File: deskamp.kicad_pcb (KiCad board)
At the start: 2 copper layers, 28 parts, among them J1 Input 01, J2 Input 02, J3 Preamp Out, J4 Selector Switch, J5 LFE, J6 Mute, J7 Sleep, J8 Motor, J9 Power, K1 Mute, K2 Sleep, K3 TQ2-12V, K4 TQ2-12V, Q1 PN2222A, Q2 PN2222A, Q3 PN2222A, Q4 PN2222A, U1 esp32-wemos-d1-mini, U2 L9110, U3 TSR_1-2433

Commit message: Stuck until modelling Alps pot
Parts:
- K1: value Mute -> TQ2-12V; footprint Relay_THT:Relay_SPDT_Panasonic_JW1_FormC -> tq2:RELAY_TQ2_PAN
- K2: value Sleep -> TQ2-12V; footprint Relay_THT:Relay_SPDT_Panasonic_JW1_FormC -> tq2:RELAY_TQ2_PAN
- moved U1 151.5 mm to (188.9, 89.1)
- moved D4 149.7 mm to (189.9, 27.0)
- moved D3 135.3 mm to (175.4, 27.0)
- moved D2 121.1 mm to (160.9, 27.0)
- moved D1 106.9 mm to (146.2, 27.0)
- moved Q4 97.4 mm to (194.2, 51.3)
- moved K4 86.1 mm to (191.4, 33.4)
- moved K3 84.0 mm to (176.8, 33.4)
- moved Q3 81.6 mm to (179.5, 52.5)
- moved U2 79.6 mm to (145.0, 111.5)
- moved K2 76.7 mm to (162.2, 33.5)
- moved U3 74.2 mm to (155.6, 85.8)
- moved R3 69.5 mm to (135.2, 88.0)
- moved Q2 67.7 mm to (165.0, 52.0)
- moved R4 66.6 mm to (133.2, 94.0)
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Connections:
- K1 pad 1: (no net) -> +12V
- K1 pad 2: (no net) -> unconnected-(K1-Pad2)
- K1 pad 4: (no net) -> Net-(J6-Pin_1)
- K1 pad 6: (no net) -> unconnected-(K1-Pad6)
- K1 pad 8: (no net) -> unconnected-(K1-Pad8)
- K2 pad 1: (no net) -> +12V
- K2 pad 2: (no net) -> Net-(J7-Pin_1)
- K2 pad 4: (no net) -> unconnected-(K2-Pad4)
- K2 pad 6: (no net) -> unconnected-(K2-Pad6)
- K2 pad 8: (no net) -> unconnected-(K2-Pad8)
- U1 pad 25: Net-(Q3-B) -> Net-(Q4-B)
- U1 pad 27: Net-(Q4-B) -> Net-(Q3-B)

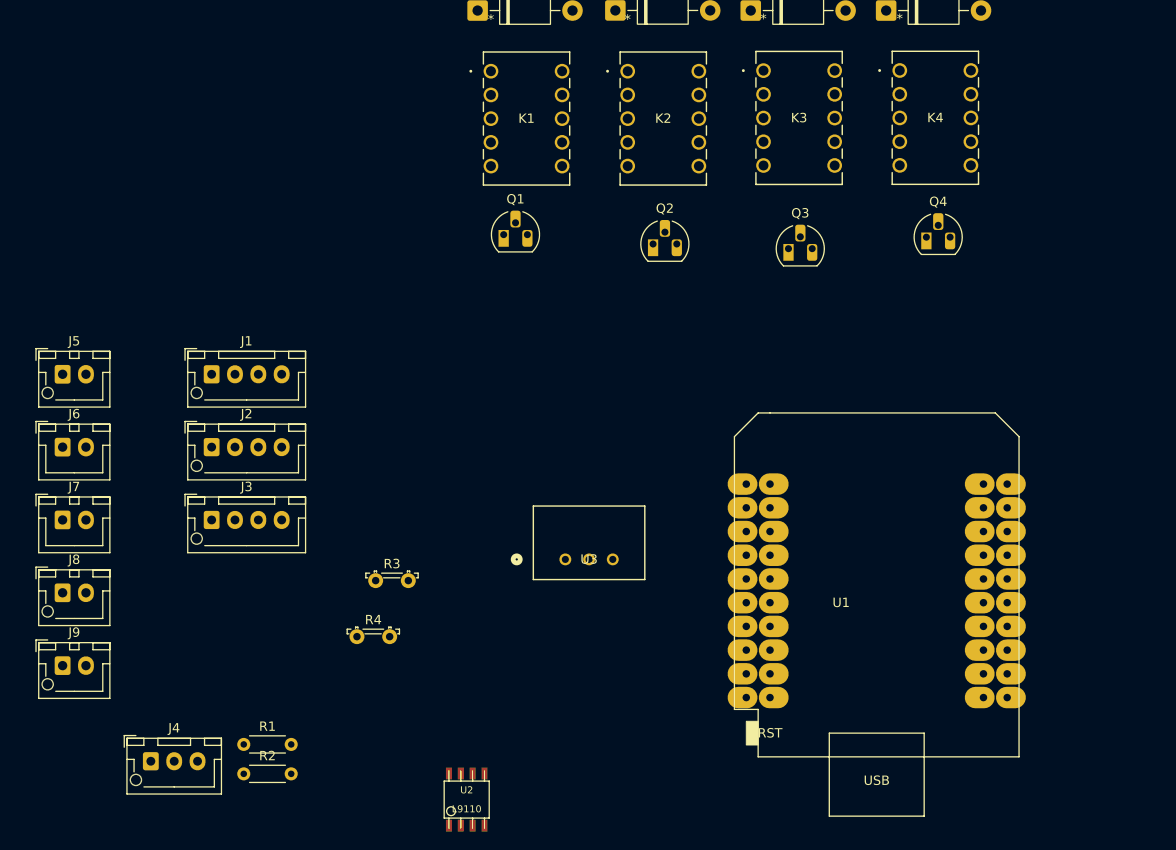
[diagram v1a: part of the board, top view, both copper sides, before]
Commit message: Use Alps RK27 as temp
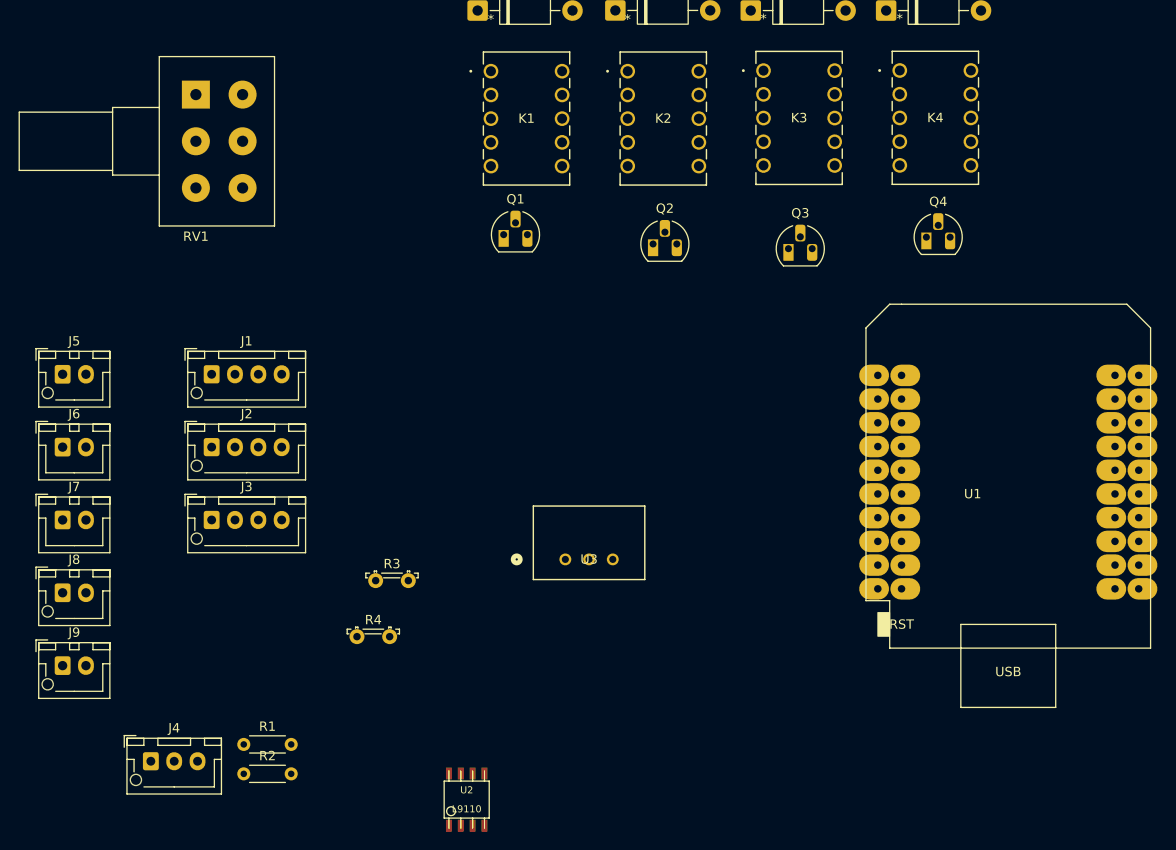
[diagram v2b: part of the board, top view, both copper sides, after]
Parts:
- added RV1: ALPS RK27, Potentiometer_THT:Potentiometer_Alps_RK163_Dual_Horizontal, F.Cu at (116.0, 36.0)
- moved U1 18.3 mm to (203.0, 77.5)

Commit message: Update deskamp.kicad_pcb
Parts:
- moved U2 79.2 mm to (98.6, 47.3)
- moved R2 75.7 mm to (97.5, 36.9)
- moved J4 75.7 mm to (87.5, 35.5)
- moved R1 75.7 mm to (97.5, 33.7)
- moved J9 53.5 mm to (155.0, 92.5)
- moved J8 44.5 mm to (88.2, 47.0)
- moved RV1 41.0 mm to (75.0, 36.2)
- moved J5 23.5 mm to (124.5, 71.8)
- moved J1 21.3 mm to (138.8, 63.0)
- moved J2 21.3 mm to (138.8, 70.8)
- moved J3 19.9 mm to (124.4, 62.9)
- moved U1 9.36 mm to (194.5, 73.5), turned to -90 degrees
- moved Q3 1.50 mm to (179.5, 51.0)
- moved Q2 1.00 mm to (165.0, 51.0)
- moved Q4 0.27 mm to (194.2, 51.0)

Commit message: More arranging
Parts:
- moved R3 59.9 mm to (75.8, 95.0), turned to 180 degrees
- moved R4 57.8 mm to (75.8, 100.0), turned to 180 degrees
- moved J3 54.0 mm to (72.5, 77.5)
- moved J5 54.0 mm to (72.6, 86.4)
- moved J1 16.5 mm to (124.2, 70.8)

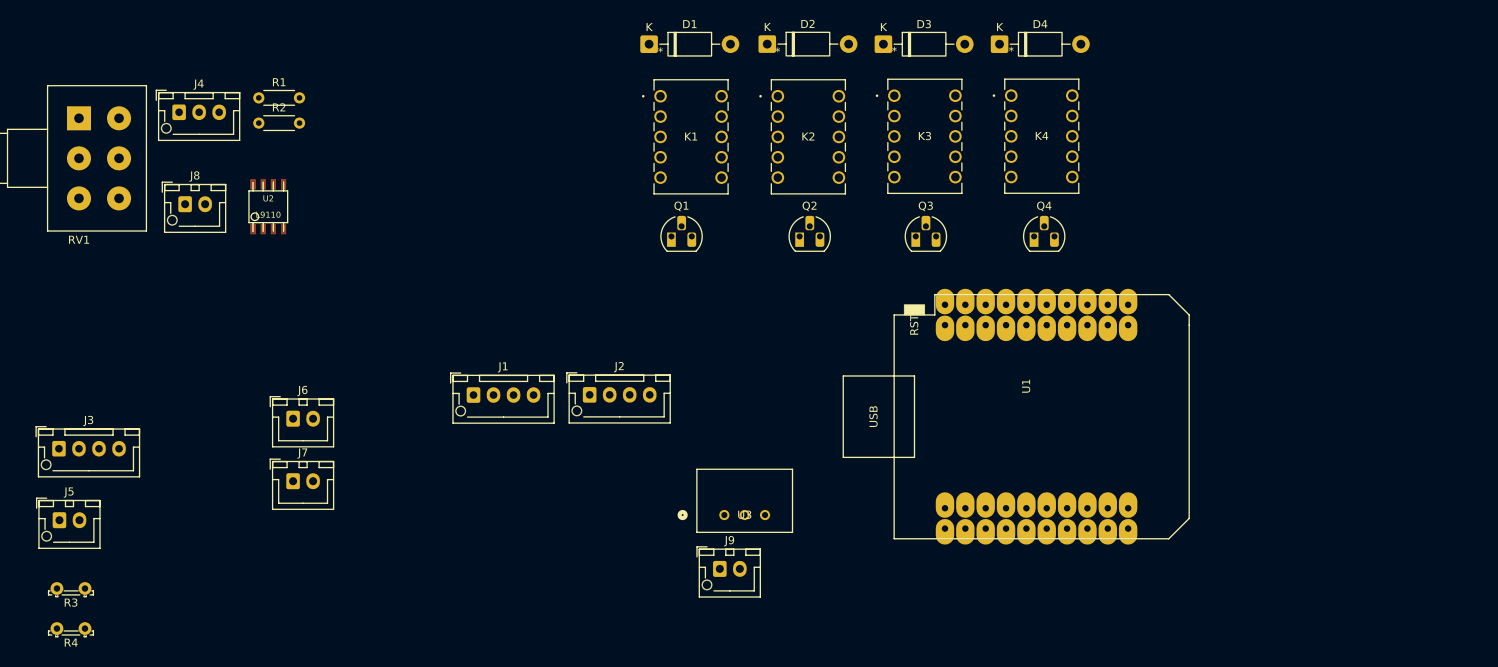
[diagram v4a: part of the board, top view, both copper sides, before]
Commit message: Add base resistors
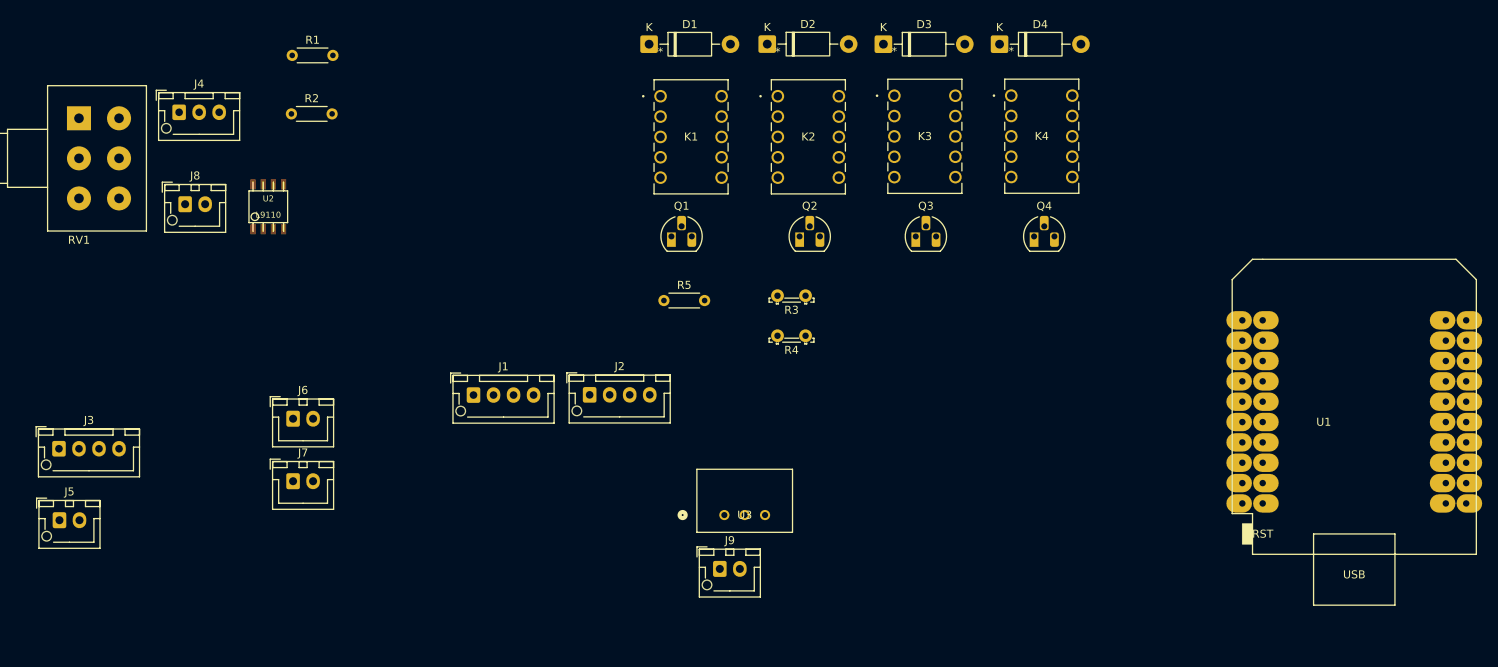
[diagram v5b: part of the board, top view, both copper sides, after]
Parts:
- added R5: 1K, Resistor_THT:R_Axial_DIN0204_L3.6mm_D1.6mm_P5.08mm_Horizontal, F.Cu at (148.0, 59.0)
- moved R3 97.1 mm to (165.7, 58.4)
- moved R4 97.1 mm to (165.7, 63.4)
- moved U1 39.7 mm to (234.2, 72.9), turned to 0 degrees
- moved R1 6.74 mm to (101.6, 28.4)
- moved R2 4.23 mm to (101.5, 35.7)
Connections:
- U1 pad 25: Net-(Q4-B) -> Net-(U1-IO_22/D1/SCL)
- U1 pad 27: Net-(Q3-B) -> Net-(U1-IO_21/D2/SDA)
- U1 pad 29: Net-(Q2-B) -> Net-(U1-IO_17/D3)
- U1 pad 31: Net-(Q1-B) -> Net-(U1-IO_16/D4)

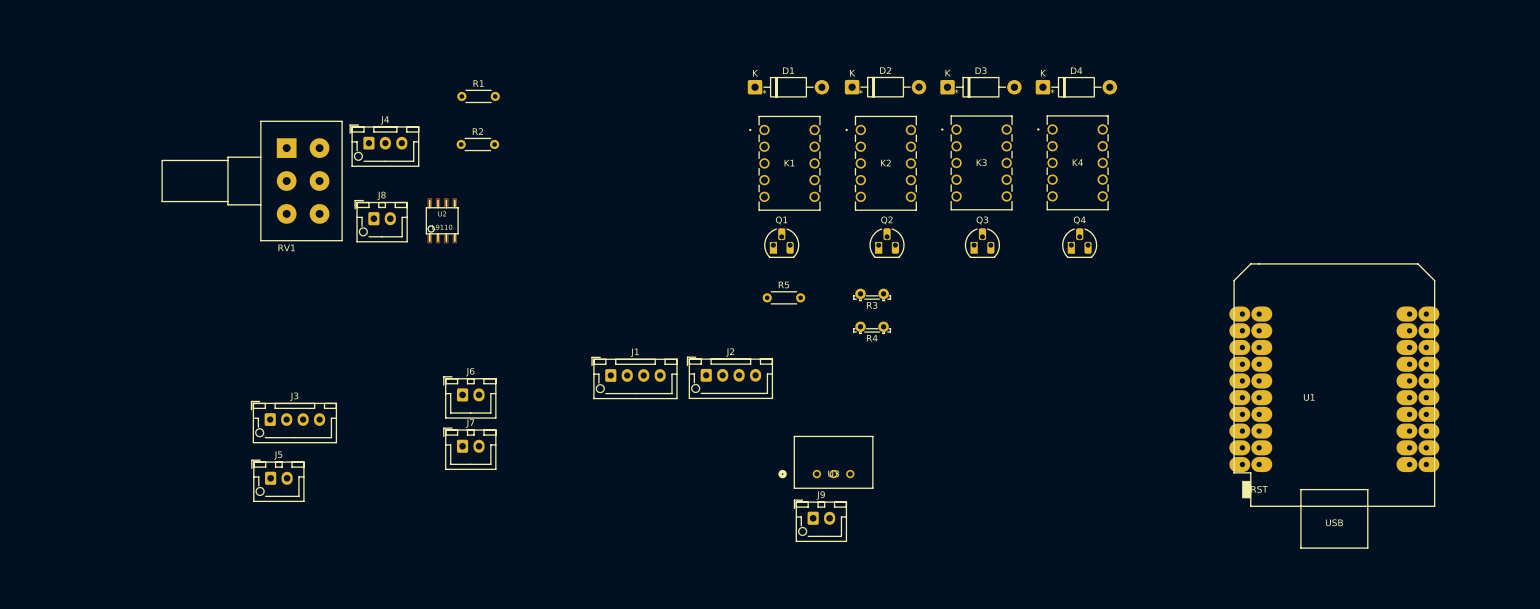
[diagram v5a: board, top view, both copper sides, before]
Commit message: Fix footprints
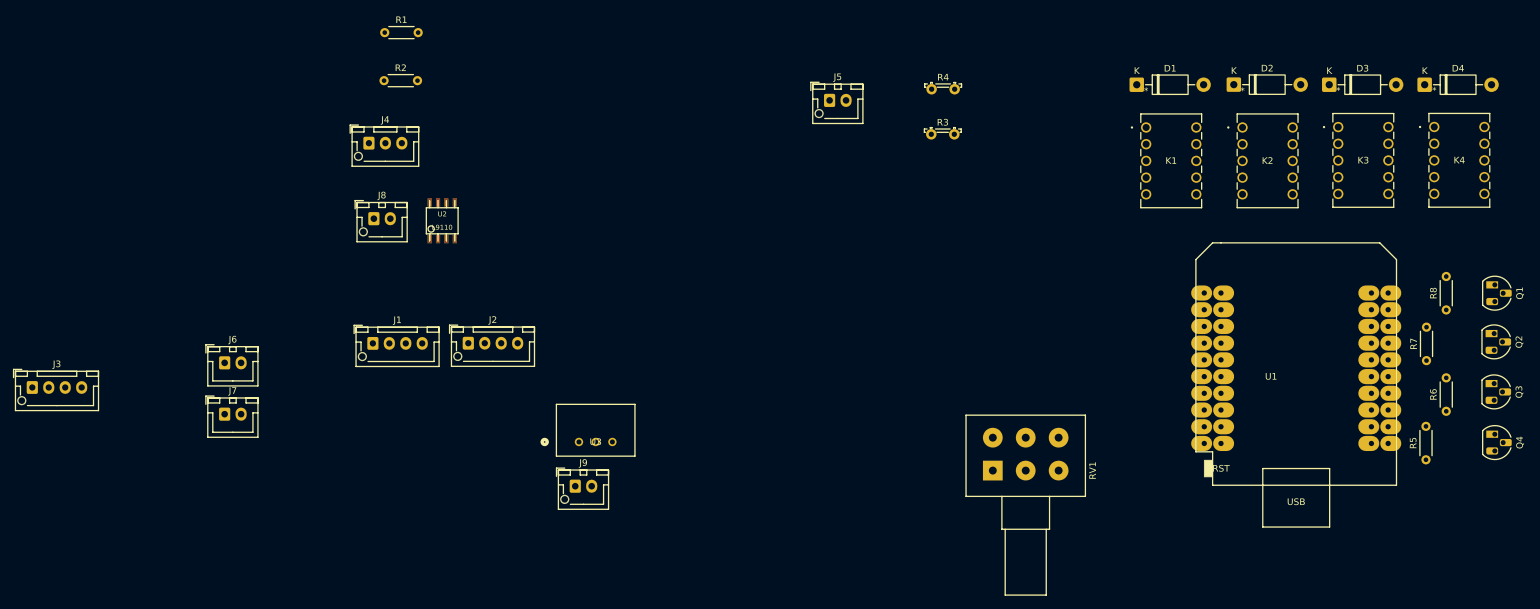
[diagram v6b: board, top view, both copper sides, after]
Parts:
- added R6: 1K, Resistor_THT:R_Axial_DIN0204_L3.6mm_D1.6mm_P5.08mm_Horizontal, F.Cu at (251.2, 76.2)
- added R7: 1K, Resistor_THT:R_Axial_DIN0204_L3.6mm_D1.6mm_P5.08mm_Horizontal, F.Cu at (248.2, 68.5)
- added R8: 1K, Resistor_THT:R_Axial_DIN0204_L3.6mm_D1.6mm_P5.08mm_Horizontal, F.Cu at (251.2, 60.8)
- moved RV1 118.0 mm to (182.3, 85.2), turned to 90 degrees
- moved Q1 109.8 mm to (258.6, 57.0), turned to -90 degrees
- moved R5 103.1 mm to (248.1, 83.6), turned to 90 degrees
- moved J5 102.5 mm to (157.5, 29.0)
- moved Q2 94.5 mm to (258.5, 64.4), turned to -90 degrees
- moved Q3 81.8 mm to (258.5, 72.0), turned to -90 degrees
- moved Q4 70.5 mm to (258.6, 79.7), turned to -90 degrees
- moved D1 58.0 mm to (204.2, 26.6)
- moved D2 58.0 mm to (218.9, 26.6)
- moved D3 58.0 mm to (233.4, 26.6)
- moved D4 58.0 mm to (247.9, 26.6)
- moved K1 58.0 mm to (205.6, 33.1)
- moved K2 58.0 mm to (220.2, 33.1)
- moved K3 58.0 mm to (234.8, 33.1)
- moved K4 58.0 mm to (249.4, 33.0)
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
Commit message: Check footprints
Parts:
- R3, R4: footprint OptoDevice:R_LDR_5.2x5.2mm_P3.5mm_Horizontal -> Resistor_THT:R_Axial_Power_L38.0mm_W9.0mm_P40.64mm
- moved J3 138.1 mm to (167.4, 29.1)
- moved J6 134.6 mm to (193.8, 27.8)
- moved J7 134.2 mm to (193.8, 37.0)
- moved U3 89.0 mm to (205.7, 59.0), turned to 90 degrees
- moved J9 85.6 mm to (202.6, 69.9)
- moved J8 84.2 mm to (166.3, 78.6)
- moved U2 74.2 mm to (169.2, 70.3)
- moved R3 38.8 mm to (138.8, 52.5)
- moved R4 37.2 mm to (138.7, 41.9)
- moved J2 18.0 mm to (88.0, 76.4)

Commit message: Add rough pot footprint (first footprint!)
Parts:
- J6, J7: footprint Connector_JST:JST_XH_B2B-XH-A_1x02_P2.50mm_Vertical -> Connector_JST:JST_XH_B2B-XH-AM_1x02_P2.50mm_Vertical
- RV1: footprint Potentiometer_THT:Potentiometer_Alps_RK163_Dual_Horizontal -> Potentiometer_THT:Potentiometer_Alps_RK27112MC
- moved R4 114.3 mm to (205.3, 134.7), turned to 90 degrees
- moved R3 112.7 mm to (216.0, 134.6), turned to 90 degrees
- moved RV1 82.2 mm to (242.8, 141.0)
- moved Q1 73.8 mm to (184.9, 54.8), turned to 0 degrees
- moved J1 68.5 mm to (20.5, 54.8), turned to 90 degrees
- moved J2 67.8 mm to (20.5, 69.8), turned to 90 degrees
- moved D1 67.5 mm to (136.8, 22.8)
- moved J3 67.5 mm to (100.0, 25.3)
- moved J5 67.5 mm to (90.1, 25.2)
- moved J6 67.5 mm to (126.4, 24.0)
- moved J7 67.5 mm to (126.4, 33.2)
- moved J9 67.5 mm to (135.2, 66.1)
- moved K1 67.5 mm to (138.2, 29.3)
- moved K2 67.5 mm to (152.8, 29.3)
- moved K3 67.5 mm to (167.4, 29.3)
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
